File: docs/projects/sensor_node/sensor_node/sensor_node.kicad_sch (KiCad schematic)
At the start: 18 parts, among them J1 Conn_01x02, J2 Conn_01x02, U1 AP2112K-3.3, U10 C_100nF_0603, U11 SHT31-DIS, U12 R_4.7k_0603, U13 R_4.7k_0603, U14 R_10k_0603, U15 R_0R_0603, U16 R_10k_0603, U2 C_10uF_0805, U3 C_10uF_0805, U4 C_100nF_0603, U5 STM32L031K6Tx, U6 C_100nF_0603, U7 C_100nF_0603, U8 C_100nF_0603, U9 C_1uF_0603

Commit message: Grid schematic layout + render guidance (fix real-symbol sprawl)
The planner placed every subsystem on one horizontal lane (x = 60 +
i*80mm), so a 7-part block ran ~540mm wide — off the A4 page — and wires
fanned across the whole canvas. Real KiCad symbols (own geometry) made it
worse.

planner.py: place subsystems on a wrapped grid instead. Cell size adapts
to the largest symbol's bbox (_symbol_extent via lib.load_symbol; fixed
fallback for synthesized parts), wrapping after _GRID_MAX_COLS. Parts are
now bounded, readable, and labeled. Wires are still point-to-point so some
crossings remain — net-aware placement / orthogonal routing is a separate,
larger effort; judge correctness from ERC, not wire aesthetics.

AGENT_GUIDE.md: document board.show() (inline per-cell render so the
engineer sees the board grow step by step) and render_sch_svg for a
standalone file — always render the final schematic, not just the zip.

Regenerate the 3 example schematics with the new layout + commit their
rendered .svg.

Co-Authored-By: Claude Opus 4.8 (1M context) <noreply@anthropic.com>
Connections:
- net GND: no longer J1.2 (Pin_2), U1.2 (GND), U10.2, U11.8 (VSS), U11.9 (VSS), U14.2, U15.2, U2.2, U3.2, U4.2, U5.16 (VSS), U5.32 (VSS), U6.2, U7.2, U8.2, U9.2
- new net: J1.2 (Pin_2), U1.2 (GND), U10.2, U11.8 (VSS), U11.9 (VSS), U14.2, U15.2, U2.2, U3.2, U4.2, U5.16 (VSS), U5.32 (VSS), U6.2, U7.2, U8.2, U9.2

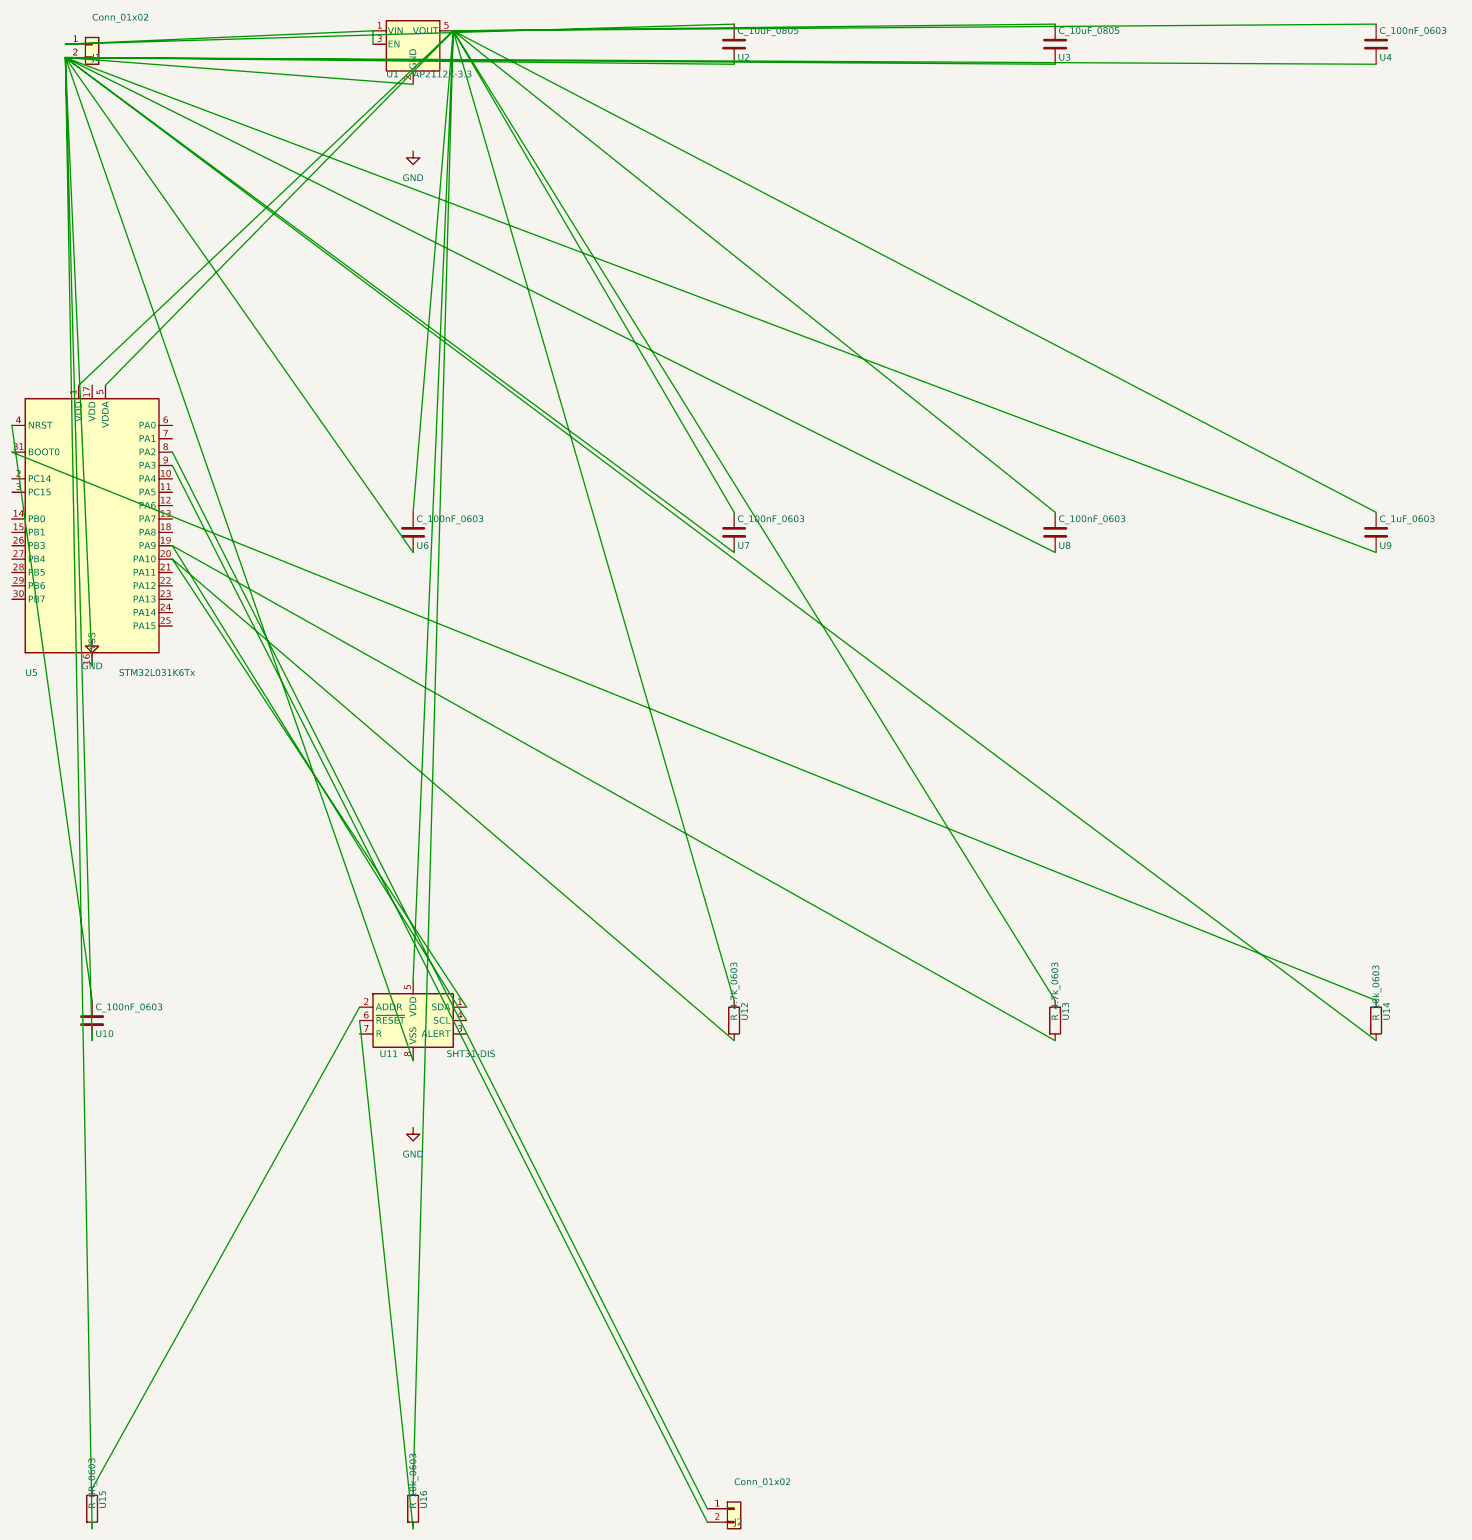
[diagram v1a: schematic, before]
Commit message: Auto-layout A1: cluster factory blocks (Buck + its passives)
Placement now groups parts that share a `group` into one tight mini-grid
block, then packs blocks left-to-right (wrapping past _PAGE_W_MM). The
Buck factory tags its IC + Cin/Cout/L/Cboot + feedback divider with
group=id, so each regulator lays out as a coherent cluster instead of its
passives scattering across the sheet — internal wires stay short and the
two bucks in power_brick read as two distinct blocks.

- SubsystemPick.group (placement cluster hint).
- _place_subsystems(): group → mini-grid per cluster, block packing with
  page-width wrap. Replaces the flat per-part grid.

This is auto-layout stage A1 (clustering). Net-aware ordering WITHIN a
cluster (A2) and an orthogonal wire router (A3) are the remaining levers
for crossing-free wiring — judge correctness from ERC, not aesthetics.

Regenerate the 3 example schematics + rendered SVGs.

Co-Authored-By: Claude Opus 4.8 (1M context) <noreply@anthropic.com>
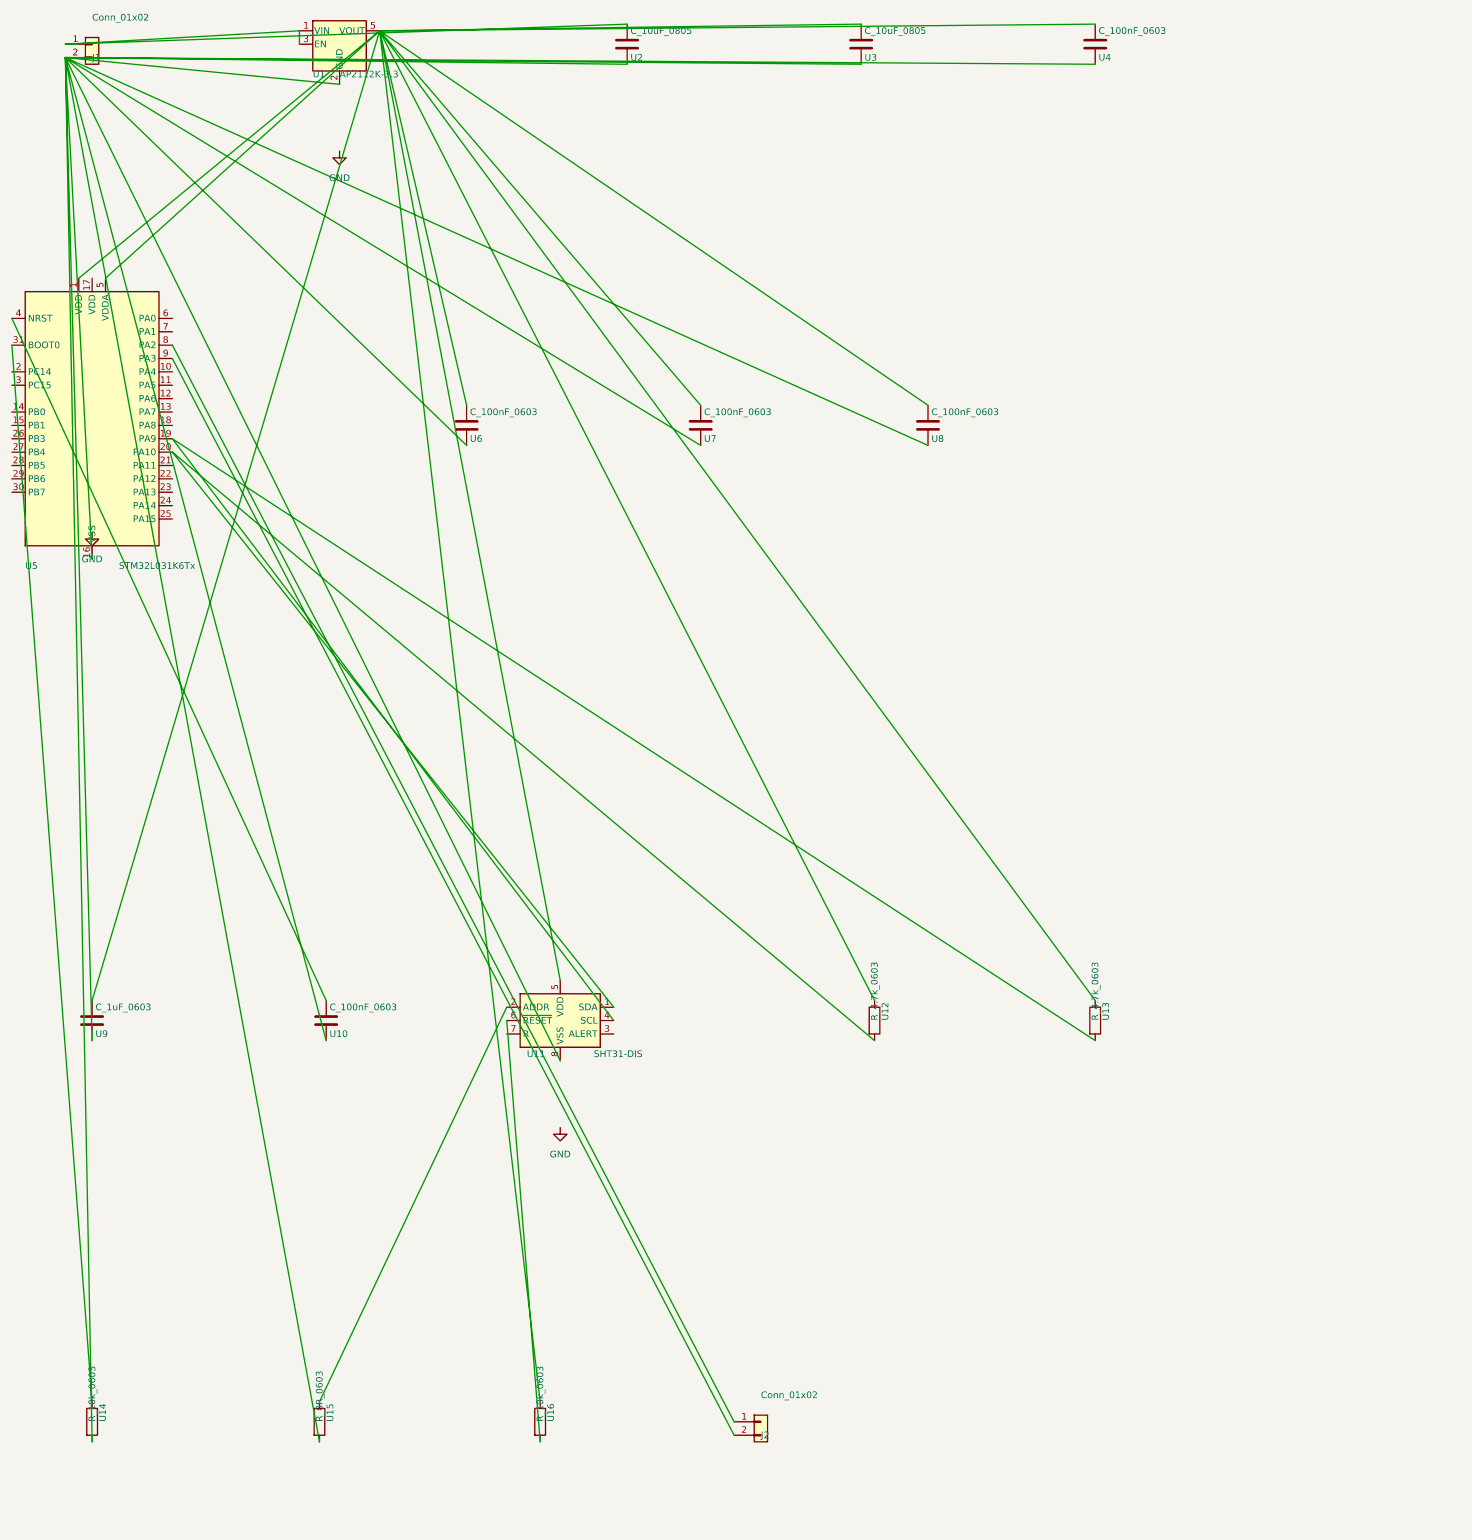
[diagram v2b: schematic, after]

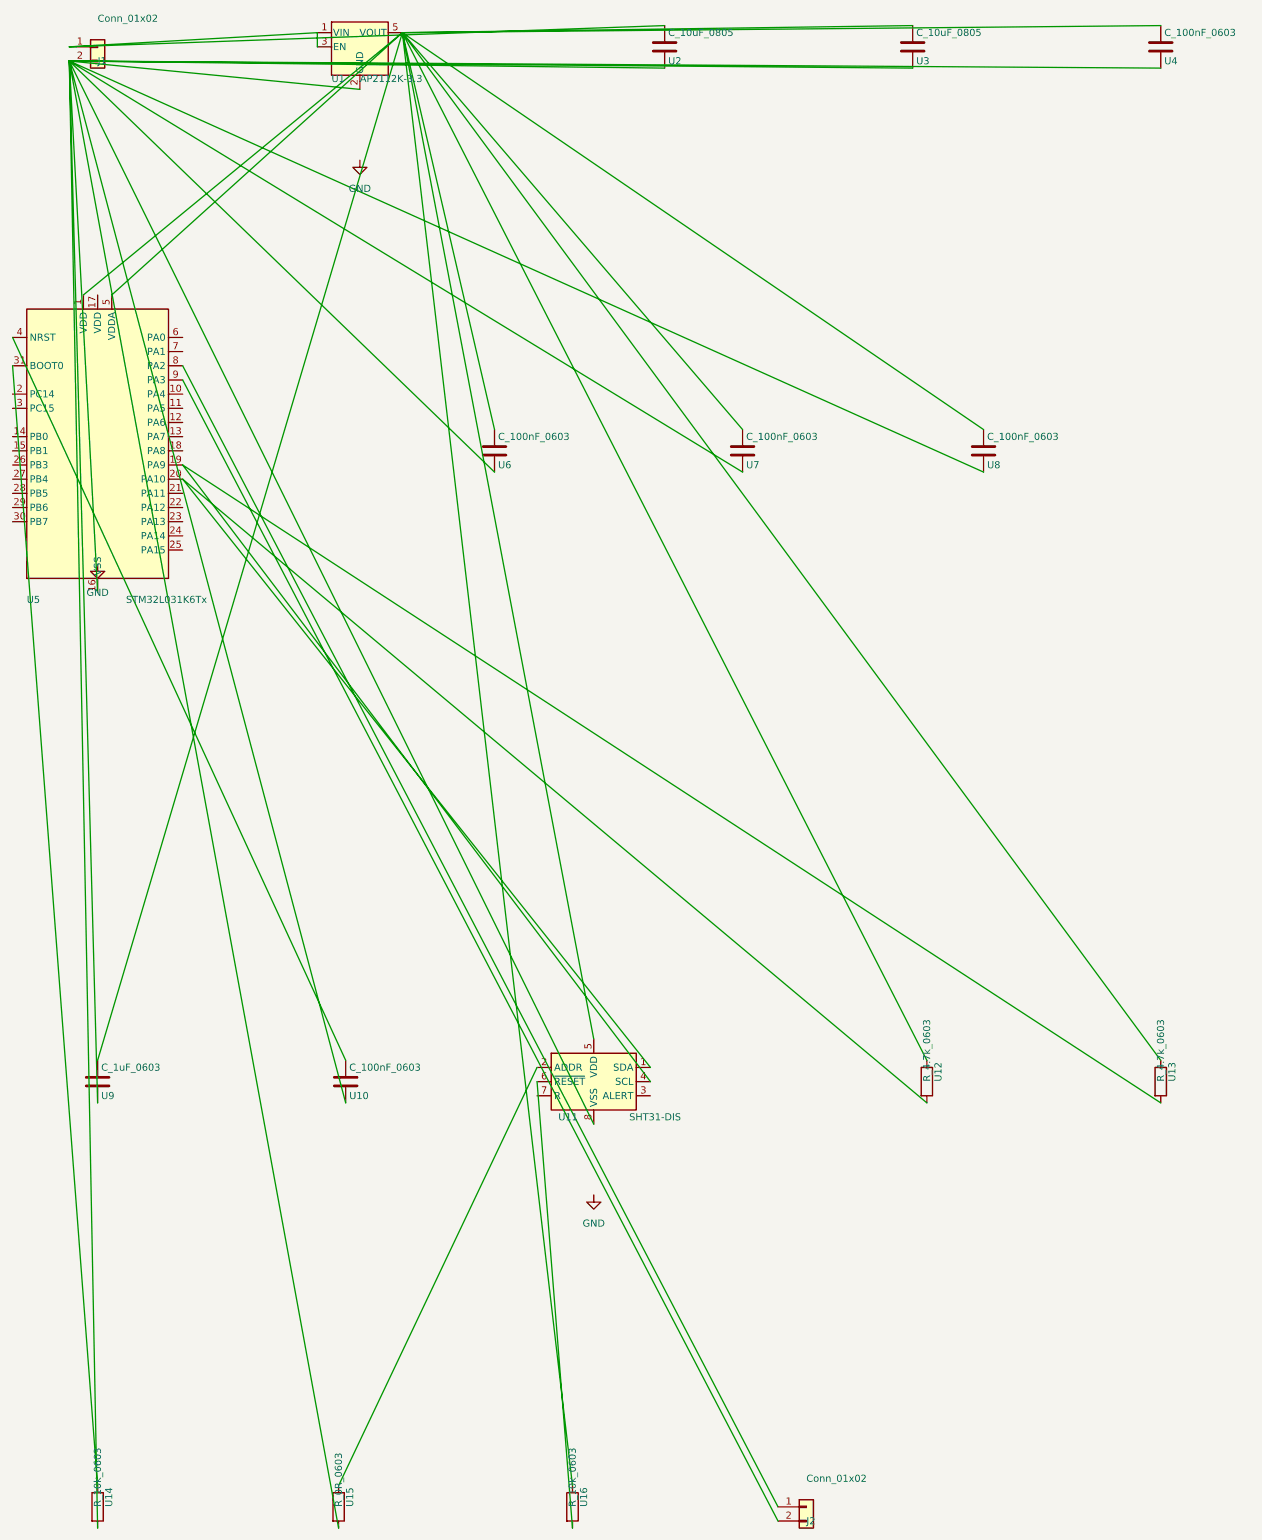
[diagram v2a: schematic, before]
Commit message: Auto-group ungrouped passives + anchor-first cluster ordering
Extend placement clustering beyond explicit factory groups: an ungrouped
passive (R/C/L) is attached to the group of the subsystem it shares the
most connections with (_effective_groups), and within each cluster the
anchor (the non-passive the group is built around) is placed first.

Effect: decoupling caps / pull-ups gather into a cluster instead of
scattering across the sheet. HONEST LIMITATION: with a flat netlist the
attachment follows the power net's star hub (usually the regulator/source),
so a cap clusters near the rail source rather than precisely beside the IC
it decouples — better than random scatter, not yet ideal.

Placement heuristics have largely plateaued here; the remaining eyesore is
point-to-point diagonal wiring. The decisive next lever is A3 (an
orthogonal wire router) or adopting ELK — not more placement tweaks.

Regenerate the 3 example schematics + SVGs.

Co-Authored-By: Claude Opus 4.8 (1M context) <noreply@anthropic.com>
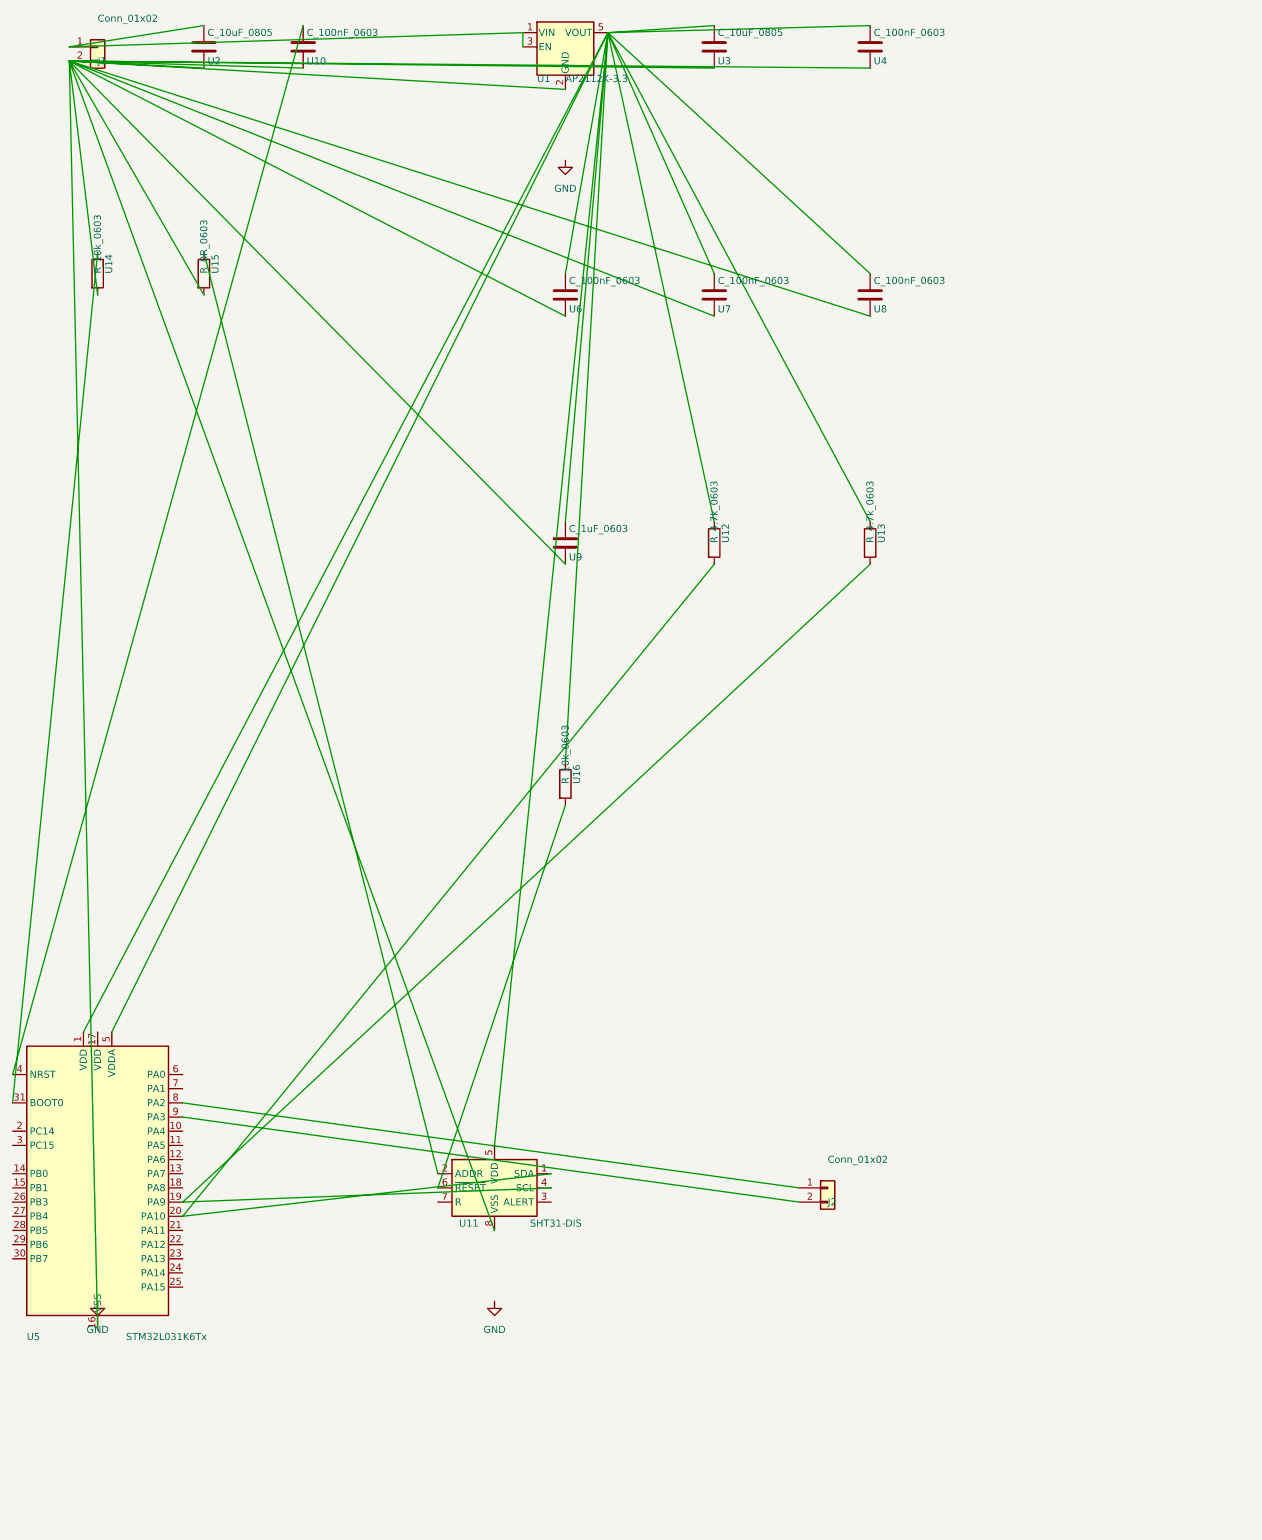
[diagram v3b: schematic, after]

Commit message: Regenerate examples + ELK layout tests
Re-execute power_brick / can_servo / sensor_node through the mandatory
ELK path; schematics now route with clean orthogonal wires that meet
pins, ERC clean (0 real / 0 expected on ERC_REAL_SYMBOL_CODES). Refresh
the tracked rendered SVGs.

Add tests/test_elk_layout.py: ELK raises LayoutError when node/the bridge
is unavailable (no fallback), and every routed wire is axis-aligned,
grid-snapped, and lands its pins on the routed endpoints.

Co-Authored-By: Claude Opus 4.8 (1M context) <noreply@anthropic.com>
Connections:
- net GND: now also J1.2 (Pin_2), U1.2 (GND), U10.2, U11.8 (VSS), U11.9 (VSS), U14.2, U15.2, U2.2, U3.2, U4.2, U5.16 (VSS), U5.32 (VSS), U6.2, U7.2, U8.2, U9.2
